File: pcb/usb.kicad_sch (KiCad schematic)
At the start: 28 parts, among them J2 USB_C_Receptacle, Q1 FDN340P, Q2 FS8025A, Q3 FDN340P, SW2 SW_SPDT, U2 TP4056-42-ESOP8, U3 DW01A

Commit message: Fill in some more components
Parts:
- BT1: footprint (none) -> Battery:BatteryHolder_Keystone_1042_1x18650
- C17: footprint (none) -> Capacitor_SMD:C_0805_2012Metric_Pad1.18x1.45mm_HandSolder
- D64: footprint (none) -> Diode_SMD:D_SMB_Handsoldering
- D68: footprint (none) -> Diode_SMD:D_MicroSMP_AK
- F1: footprint (none) -> Fuse:Fuse_0402_1005Metric_Pad0.77x0.64mm_HandSolder
- Q1, Q3: footprint Package_TO_SOT_SMD:SOT-23 -> Package_TO_SOT_SMD:SOT-23_Handsoldering
- Q2: footprint (none) -> Package_TO_SOT_SMD:SOT-23-6_Handsoldering
- R3, R8, R9: footprint (none) -> Resistor_SMD:R_0805_2012Metric_Pad1.20x1.40mm_HandSolder
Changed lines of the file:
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@@
 		)
 		(instances
-			(project ""
+			(project "keyboard"
 				(path "/39e5e398-89ad-4475-a3bf-05d3324a2c58/10482084-a545-4aa4-8b75-11043176cfae"
 					(reference "U3")
@@
 		)
 		(instances
-			(project ""
+			(project "keyboard"
 				(path "/39e5e398-89ad-4475-a3bf-05d3324a2c58/10482084-a545-4aa4-8b75-11043176cfae"
 					(reference "#PWR027")
@@
 		)
 		(instances
-			(project ""
+			(project "keyboard"
 				(path "/39e5e398-89ad-4475-a3bf-05d3324a2c58/10482084-a545-4aa4-8b75-11043176cfae"
 					(reference "TH1")
@@
 		)
 		(instances
-			(project ""
+			(project "keyboard"
 				(path "/39e5e398-89ad-4475-a3bf-05d3324a2c58/10482084-a545-4aa4-8b75-11043176cfae"
 					(reference "#PWR020")
@@
 		)
 		(instances
-			(project ""
+			(project "keyboard"
 				(path "/39e5e398-89ad-4475-a3bf-05d3324a2c58/10482084-a545-4aa4-8b75-11043176cfae"
 					(reference "SW2")
@@
 			)
 		)
-		(property "Footprint" ""
+		(property "Footprint" "Diode_SMD:D_SMB_Handsoldering"
 			(at 185.42 121.92 0)
 			(effects
@@
 		)
 		(instances
-			(project ""
+			(project "keyboard"
 				(path "/39e5e398-89ad-4475-a3bf-05d3324a2c58/10482084-a545-4aa4-8b75-11043176cfae"
 					(reference "D64")
@@
 			)
 		)
-		(property "Footprint" ""
+		(property "Footprint" "Package_TO_SOT_SMD:SOT-23-6_Handsoldering"
 			(at 232.41 144.78 0)
 			(effects
@@
 		)
 		(instances
-			(project ""
+			(project "keyboard"
 				(path "/39e5e398-89ad-4475-a3bf-05d3324a2c58/10482084-a545-4aa4-8b75-11043176cfae"
 					(reference "Q2")
@@
 		)
 		(instances
-			(project ""
+			(project "keyboard"
 				(path "/39e5e398-89ad-4475-a3bf-05d3324a2c58/10482084-a545-4aa4-8b75-11043176cfae"
 					(reference "C11")
@@
 			)
 		)
-		(property "Footprint" ""
+		(property "Footprint" "Fuse:Fuse_0402_1005Metric_Pad0.77x0.64mm_HandSolder"
 			(at 165.862 123.19 90)
 			(effects
@@
 		)
 		(instances
-			(project ""
+			(project "keyboard"
 				(path "/39e5e398-89ad-4475-a3bf-05d3324a2c58/10482084-a545-4aa4-8b75-11043176cfae"
 					(reference "F1")
@@
 		)
 		(instances
-			(project ""
+			(project "keyboard"
 				(path "/39e5e398-89ad-4475-a3bf-05d3324a2c58/10482084-a545-4aa4-8b75-11043176cfae"
 					(reference "R4")
@@
 			)
 		)
-		(property "Footprint" ""
+		(property "Footprint" "Resistor_SMD:R_0805_2012Metric_Pad1.20x1.40mm_HandSolder"
 			(at 176.022 134.62 90)
 			(effects
@@
 		)
 		(instances
-			(project ""
+			(project "keyboard"
 				(path "/39e5e398-89ad-4475-a3bf-05d3324a2c58/10482084-a545-4aa4-8b75-11043176cfae"
 					(reference "R3")
@@
 			)
 		)
-		(property "Footprint" ""
+		(property "Footprint" "Diode_SMD:D_MicroSMP_AK"
 			(at 137.16 109.22 0)
 			(effects
@@
 		)
 		(instances
-			(project ""
+			(project "keyboard"
 				(path "/39e5e398-89ad-4475-a3bf-05d3324a2c58/10482084-a545-4aa4-8b75-11043176cfae"
 					(reference "R6")
@@
 		)
 		(instances
-			(project ""
+			(project "keyboard"
 				(path "/39e5e398-89ad-4475-a3bf-05d3324a2c58/10482084-a545-4aa4-8b75-11043176cfae"
 					(reference "U2")
@@
 		)
 		(instances
-			(project ""
+			(project "keyboard"
 				(path "/39e5e398-89ad-4475-a3bf-05d3324a2c58/10482084-a545-4aa4-8b75-11043176cfae"
 					(reference "#PWR029")
@@
 			)
 		)
-		(property "Footprint" ""
+		(property "Footprint" "Resistor_SMD:R_0805_2012Metric_Pad1.20x1.40mm_HandSolder"
 			(at 213.36 114.808 90)
 			(effects
@@
 		)
 		(instances
-			(project ""
+			(project "keyboard"
 				(path "/39e5e398-89ad-4475-a3bf-05d3324a2c58/10482084-a545-4aa4-8b75-11043176cfae"
 					(reference "R8")
@@
 			)
 		)
-		(property "Footprint" "Package_TO_SOT_SMD:SOT-23"
+		(property "Footprint" "Package_TO_SOT_SMD:SOT-23_Handsoldering"
 			(at 179.705 113.03 0)
 			(effects
@@
 			)
 		)
-		(property "Footprint" ""
+		(property "Footprint" "Resistor_SMD:R_0805_2012Metric_Pad1.20x1.40mm_HandSolder"
 			(at 252.222 130.81 90)
 			(effects
@@
 		)
 		(instances
-			(project ""
+			(project "keyboard"
 				(path "/39e5e398-89ad-4475-a3bf-05d3324a2c58/10482084-a545-4aa4-8b75-11043176cfae"
 					(reference "R9")
@@
 		)
 		(instances
-			(project ""
+			(project "keyboard"
 				(path "/39e5e398-89ad-4475-a3bf-05d3324a2c58/10482084-a545-4aa4-8b75-11043176cfae"
 					(reference "J2")
@@
 			)
 		)
-		(property "Footprint" ""
+		(property "Footprint" "Battery:BatteryHolder_Keystone_1042_1x18650"
 			(at 167.64 134.366 90)
 			(effects
@@
 		)
 		(instances
-			(project ""
+			(project "keyboard"
 				(path "/39e5e398-89ad-4475-a3bf-05d3324a2c58/10482084-a545-4aa4-8b75-11043176cfae"
 					(reference "BT1")
@@
 		)
 		(instances
-			(project ""
+			(project "keyboard"
 				(path "/39e5e398-89ad-4475-a3bf-05d3324a2c58/10482084-a545-4aa4-8b75-11043176cfae"
 					(reference "#PWR023")
@@
 			)
 		)
-		(property "Footprint" ""
+		(property "Footprint" "Capacitor_SMD:C_0805_2012Metric_Pad1.18x1.45mm_HandSolder"
 			(at 220.6752 125.73 0)
 			(effects
@@
 		)
 		(instances
-			(project ""
+			(project "keyboard"
 				(path "/39e5e398-89ad-4475-a3bf-05d3324a2c58/10482084-a545-4aa4-8b75-11043176cfae"
 					(reference "C17")
@@
 			)
 		)
-		(property "Footprint" "Package_TO_SOT_SMD:SOT-23"
+		(property "Footprint" "Package_TO_SOT_SMD:SOT-23_Handsoldering"
 			(at 129.54 114.935 0)
 			(effects
@@
 		)
 		(instances
-			(project ""
+			(project "keyboard"
 				(path "/39e5e398-89ad-4475-a3bf-05d3324a2c58/10482084-a545-4aa4-8b75-11043176cfae"
 					(reference "#PWR019")
@@
 		)
 		(instances
-			(project ""
+			(project "keyboard"
 				(path "/39e5e398-89ad-4475-a3bf-05d3324a2c58/10482084-a545-4aa4-8b75-11043176cfae"
 					(reference "D44")
@@
 		)
 		(instances
-			(project ""
+			(project "keyboard"
 				(path "/39e5e398-89ad-4475-a3bf-05d3324a2c58/10482084-a545-4aa4-8b75-11043176cfae"
 					(reference "D65")
@@
 		)
 		(instances
-			(project ""
+			(project "keyboard"
 				(path "/39e5e398-89ad-4475-a3bf-05d3324a2c58/10482084-a545-4aa4-8b75-11043176cfae"
 					(reference "#PWR028")

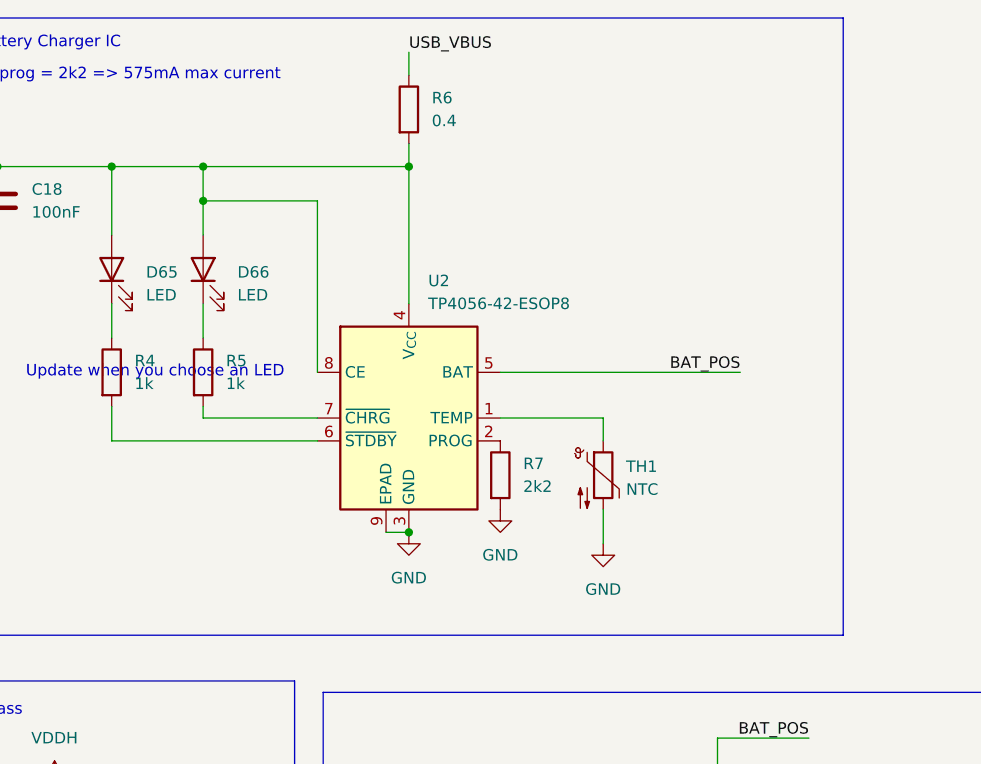
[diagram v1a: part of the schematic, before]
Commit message: Pick a battery and add extra parts for TP4056
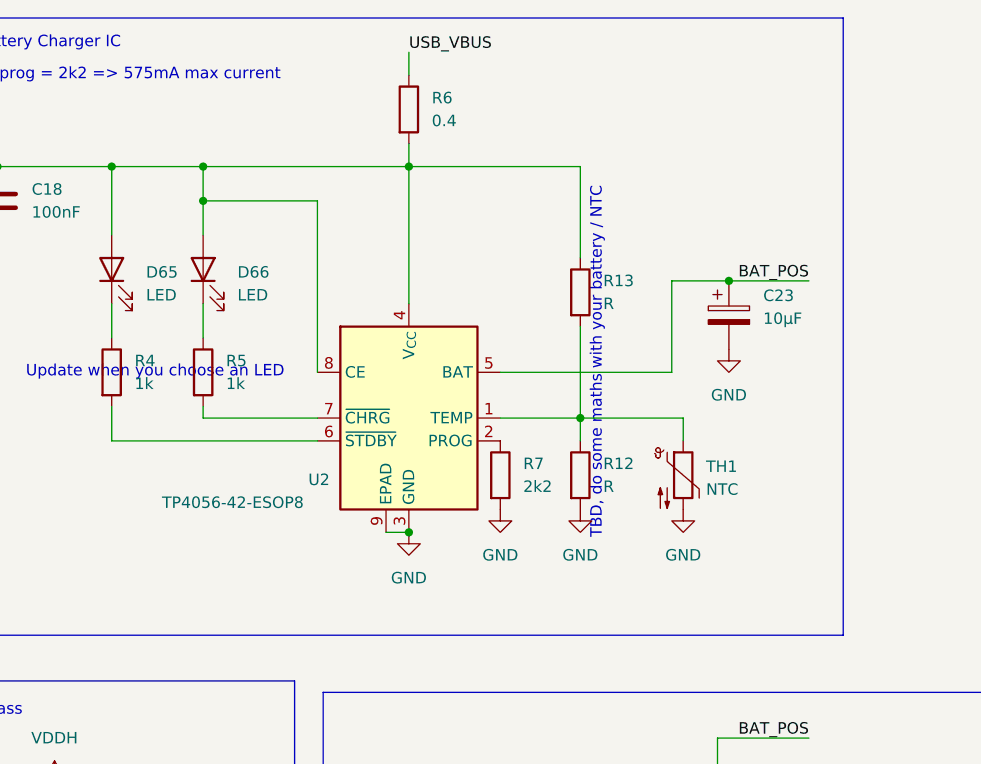
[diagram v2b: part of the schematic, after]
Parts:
- added C23: 10µF, Capacitor_Tantalum_SMD:CP_EIA-2012-15_AVX-P_HandSolder, symbol Device:C_Polarized
- added R12, R13: R, Resistor_SMD:R_0805_2012Metric_Pad1.20x1.40mm_HandSolder, symbol Device:R
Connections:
- net BAT_POS: now also C23.1
- net GND: now also C23.2, R12.2
- net at TH1.1, U2.1 (TEMP): now also R12.1, R13.2
- net at C11.1, C18.1, D65.2 (A)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: now also R13.1
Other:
- note added: "TBD, do some maths with your battery / NTC"
- moved on the sheet: TH1

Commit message: Update to kicad 10
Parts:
- D68: footprint Diode_SMD:D_MicroSMP_AK -> Diode_SMD:D_MicroSMP_LargeCathode

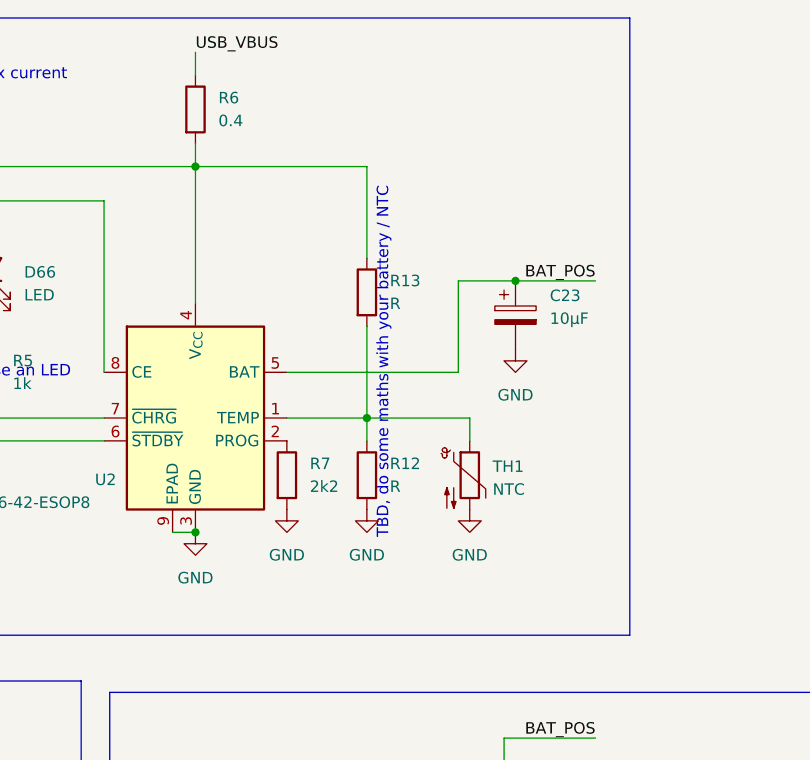
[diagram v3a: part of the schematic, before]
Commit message: Pick an NTC and calculate R1/R2
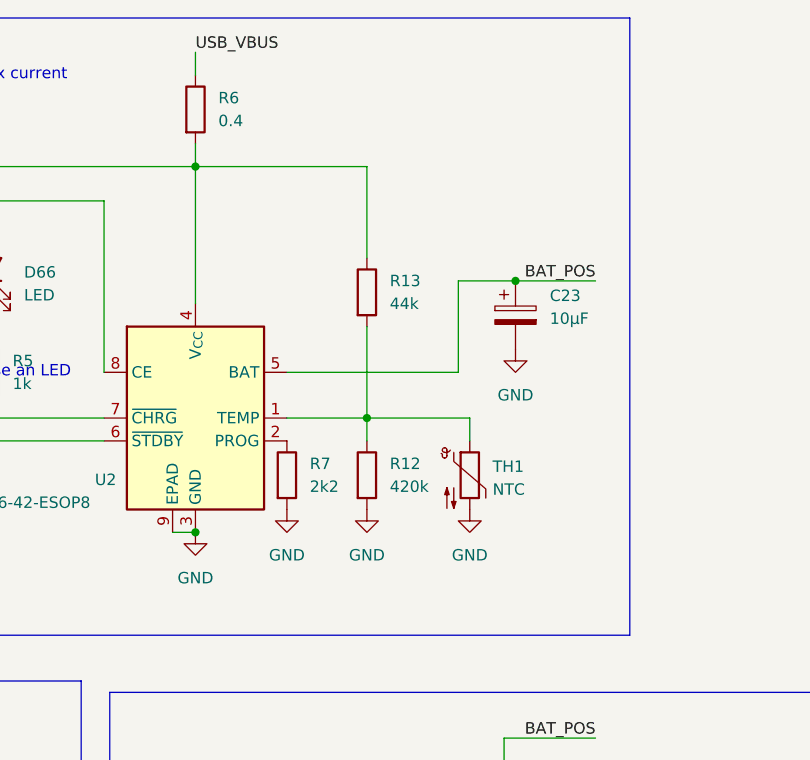
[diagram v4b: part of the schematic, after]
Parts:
- R12: value R -> 420k
- R13: value R -> 44k
- TH1: footprint (none) -> Resistor_SMD:R_0805_2012Metric_Pad1.20x1.40mm_HandSolder
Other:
- note removed: "TBD, do some maths with your battery / NTC"
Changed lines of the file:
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@@
 		)
 	)
-	(text "TBD, do some maths with your battery / NTC"
-		(exclude_from_sim no)
-		(at 192.278 59.944 90)
-		(effects
-			(font
-				(size 1.27 1.27)
-			)
-		)
-	)
 	(text "Rprog = 2k2 => 575mA max current"
 		(exclude_from_sim no)
@@
 			)
 		)
-		(property "Footprint" ""
+		(property "Footprint" "Resistor_SMD:R_0805_2012Metric_Pad1.20x1.40mm_HandSolder"
 			(at 201.93 71.12 0)
 			(hide yes)
@@
 			)
 		)
-		(property "Value" "R"
+		(property "Value" "420k"
 			(at 193.04 73.6599 0)
 			(show_name no)
@@
 			)
 		)
-		(property "Value" "R"
+		(property "Value" "44k"
 			(at 193.04 53.3399 0)
 			(show_name no)

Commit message: Did a bunch of stuff lol
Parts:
- removed J2: USB_C_Receptacle, symbol Connector:USB_C_Receptacle
- removed SW2: SW_SPDT, symbol Switch:SW_SPDT
- added J2: USB_C_Receptacle_USB2.0_16P, My_Footprints:USB_C_Receptacle_G-Switch_GT-USB-7010ASV_handsolder_lmao.csv, symbol Connector:USB_C_Receptacle_USB2.0_16P
- added SW2: SW_SPST, My_Footprints:Legion SS11, symbol Switch:SW_SPST
- C17, C18: footprint Capacitor_SMD:C_0805_2012Metric_Pad1.18x1.45mm_HandSolder -> Capacitor_SMD:C_0603_1608Metric_Pad1.08x0.95mm_HandSolder
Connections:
- net BAT_POS: now also SW2.2 (B)
- net GND: now also J2.A1 (GND), J2.A12 (GND), J2.B1 (GND), J2.B12 (GND), J2.SH (SHIELD)
- net USB_D+: now also J2.A6 (D+), J2.B6 (D+)
- net USB_D-: now also J2.A7 (D-), J2.B7 (D-)
- net USB_VBUS: now also J2.A4 (VBUS), J2.A9 (VBUS), J2.B4 (VBUS), J2.B9 (VBUS)
- net at D64.1 (K), Q1.2 (S): now also SW2.1 (A)
- net at R1.1: now also J2.A5 (CC1)
- net at R2.1: now also J2.B5 (CC2)
- no-connect marks 13 -> 4
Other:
- moved on the sheet: R1, R2, R8

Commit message: Did some stuff
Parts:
- R4, R5: footprint Resistor_SMD:R_0805_2012Metric_Pad1.20x1.40mm_HandSolder -> Resistor_SMD:R_0603_1608Metric_Pad0.98x0.95mm_HandSolder
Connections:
- net BAT_POS: now also D64.1 (K), Q1.2 (S); no longer SW2.2 (B)
- net at F1.1: now also SW2.2 (B); no longer Q1.3 (D)
- net at BT1.1 (+): now also SW2.1 (A); no longer F1.2
- new net: F1.2, Q1.3 (D)
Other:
- moved on the sheet: BT1, D64, Q1, R3

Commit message: Did a bunch of things!
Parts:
- D65, D66: footprint LED_SMD:LED_0805_2012Metric_Pad1.15x1.40mm_HandSolder -> LED_SMD:LED_0603_1608Metric_Pad1.05x0.95mm_HandSolder
- U2: footprint Package_SO:SOIC-8-1EP_3.9x4.9mm_P1.27mm_EP2.41x3.3mm_ThermalVias -> Package_SO:SOIC-8-1EP_3.9x4.9mm_P1.27mm_EP2.29x3mm
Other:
- note removed: "Update when you choose an LED"
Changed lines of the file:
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@@
 		)
 	)
-	(text "Update when you choose an LED"
-		(exclude_from_sim no)
-		(at 143.256 60.96 0)
-		(effects
-			(font
-				(size 1.27 1.27)
-			)
-		)
-	)
 	(text "Battery Charger IC"
 		(exclude_from_sim no)
@@
 			)
 		)
-		(property "Footprint" "LED_SMD:LED_0805_2012Metric_Pad1.15x1.40mm_HandSolder"
+		(property "Footprint" "LED_SMD:LED_0603_1608Metric_Pad1.05x0.95mm_HandSolder"
 			(at 148.59 49.53 0)
 			(hide yes)
@@
 			)
 		)
-		(property "Footprint" "Package_SO:SOIC-8-1EP_3.9x4.9mm_P1.27mm_EP2.41x3.3mm_ThermalVias"
+		(property "Footprint" "Package_SO:SOIC-8-1EP_3.9x4.9mm_P1.27mm_EP2.29x3mm"
 			(at 171.958 88.9 0)
 			(hide yes)
@@
 			)
 		)
-		(property "Footprint" "LED_SMD:LED_0805_2012Metric_Pad1.15x1.40mm_HandSolder"
+		(property "Footprint" "LED_SMD:LED_0603_1608Metric_Pad1.05x0.95mm_HandSolder"
 			(at 138.43 49.53 0)
 			(hide yes)
